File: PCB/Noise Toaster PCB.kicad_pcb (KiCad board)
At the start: 2 copper layers, 132.1 x 68.6 mm, 138 parts, among them Q1 2N5457, Q10 2N3906, Q2 2N3904, Q3 2N3904, Q4 2N3904, Q5 2N3904, Q6 2N3904, Q7 2N5457, Q8 2N5457, Q9 2N5457, U1 LM324, U2 LM324, U3 LM386, X4 WNS

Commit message: Shuffle things around
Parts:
- moved R6 0.76 mm to (182.3, 134.1)
- moved R41 0.63 mm to (113.7, 112.4)
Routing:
- net Net-(D1-A): track 37.5 -> 33.2 mm
- net /Attack Release Envelope Generator/X19: track 46.3 -> 42.2 mm
- net Net-(Q1-G): track 37.9 -> 38.7 mm
- net Net-(Q7-G): track 18.8 -> 19.4 mm
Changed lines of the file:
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@@
 	(footprint "Resistor_THT:R_Axial_DIN0207_L6.3mm_D2.5mm_P10.16mm_Horizontal"
 		(layer "F.Cu")
-		(at 182.276 133.377 180)
+		(at 182.276 134.139 180)
 		(descr "Resistor, Axial_DIN0207 series, Axial, Horizontal, pin pitch=10.16mm, 0.25W = 1/4W, length*diameter=6.3*2.5mm^2, http://cdn-reichelt.de/documents/datenblatt/B400/1_4W%23YAG.pdf")
 		(tags "Resistor Axial_DIN0207 series Axial Horizontal pin pitch 10.16mm 0.25W = 1/4W length 6.3mm diameter 2.5mm")
@@
 	(footprint "Resistor_THT:R_Axial_DIN0207_L6.3mm_D2.5mm_P10.16mm_Horizontal"
 		(layer "F.Cu")
-		(at 113.061 112.422 180)
+		(at 113.696 112.422 180)
 		(descr "Resistor, Axial_DIN0207 series, Axial, Horizontal, pin pitch=10.16mm, 0.25W = 1/4W, length*diameter=6.3*2.5mm^2, http://cdn-reichelt.de/documents/datenblatt/B400/1_4W%23YAG.pdf")
 		(tags "Resistor Axial_DIN0207 series Axial Horizontal pin pitch 10.16mm 0.25W = 1/4W length 6.3mm diameter 2.5mm")
@@
 	)
 	(segment
-		(start 94.011 104.167)
-		(end 98.456 108.612)
+		(start 81.057 103.405)
+		(end 84.201 103.405)
 		(width 0.5)
 		(layer "F.Cu")
@@
 	)
 	(segment
-		(start 94.011 102.897)
-		(end 94.011 104.167)
+		(start 100.107 108.612)
+		(end 102.647 111.152)
 		(width 0.5)
 		(layer "F.Cu")
@@
 	)
 	(segment
-		(start 91.598 100.484)
-		(end 94.011 102.897)
+		(start 98.456 108.612)
+		(end 100.107 108.612)
 		(width 0.5)
 		(layer "F.Cu")
@@
 	)
 	(segment
-		(start 111.791 111.152)
-		(end 113.061 112.422)
+		(start 94.011 104.167)
+		(end 98.456 108.612)
 		(width 0.5)
 		(layer "F.Cu")
@@
 	)
 	(segment
-		(start 81.057 103.405)
-		(end 84.201 103.405)
+		(start 102.647 111.152)
+		(end 112.426 111.152)
 		(width 0.5)
 		(layer "F.Cu")
@@
 	)
 	(segment
-		(start 98.456 108.612)
-		(end 100.361 108.612)
+		(start 91.598 102.262)
+		(end 91.598 100.484)
 		(width 0.5)
 		(layer "F.Cu")
@@
 	)
 	(segment
-		(start 91.598 102.262)
-		(end 91.598 100.484)
+		(start 89.693 104.167)
+		(end 91.598 102.262)
 		(width 0.5)
 		(layer "F.Cu")
@@
 	)
 	(segment
-		(start 89.693 104.167)
-		(end 91.598 102.262)
+		(start 112.426 111.152)
+		(end 113.696 112.422)
 		(width 0.5)
 		(layer "F.Cu")
@@
 	)
 	(segment
-		(start 84.963 104.167)
-		(end 89.693 104.167)
+		(start 94.011 102.897)
+		(end 94.011 104.167)
 		(width 0.5)
 		(layer "F.Cu")
@@
 	)
 	(segment
-		(start 100.361 108.612)
-		(end 102.901 111.152)
+		(start 84.963 104.167)
+		(end 89.693 104.167)
 		(width 0.5)
 		(layer "F.Cu")
@@
 	)
 	(segment
-		(start 102.901 111.152)
-		(end 111.791 111.152)
+		(start 91.598 100.484)
+		(end 94.011 102.897)
 		(width 0.5)
 		(layer "F.Cu")
@@
 	(segment
 		(start 114.331 112.422)
-		(end 113.061 112.422)
+		(end 113.696 112.422)
 		(width 0.5)
 		(layer "B.Cu")
@@
 	)
 	(segment
-		(start 113.061 112.422)
-		(end 113.676 113.037)
+		(start 121.316 105.437)
+		(end 114.331 112.422)
 		(width 0.5)
 		(layer "B.Cu")
@@
 	)
 	(segment
-		(start 113.676 124.507)
-		(end 112.426 125.757)
+		(start 113.676 112.442)
+		(end 113.676 124.507)
 		(width 0.5)
 		(layer "B.Cu")
@@
 	)
 	(segment
-		(start 113.676 113.037)
-		(end 113.676 124.507)
+		(start 113.696 112.422)
+		(end 113.676 112.442)
 		(width 0.5)
 		(layer "B.Cu")
@@
 	)
 	(segment
-		(start 121.316 105.437)
-		(end 114.331 112.422)
+		(start 113.676 124.507)
+		(end 112.426 125.757)
 		(width 0.5)
 		(layer "B.Cu")
@@
 	)
 	(segment
-		(start 184.8922 119.915)
-		(end 181.2346 119.915)
-		(width 0.5)
-		(layer "F.Cu")
-		(net "/G2")
-	)
-	(segment
 		(start 160.686 105.564)
 		(end 156.027 105.564)
@@
 	)
 	(segment
+		(start 181.2346 119.915)
+		(end 184.8922 119.915)
+		(width 0.5)
+		(layer "B.Cu")
+		(net "/G2")
+	)
+	(segment
 		(start 175.291 104.167)
 		(end 175.291 111.787)
@@
 	)
 	(segment
-		(start 187.229 113.565)
+		(start 183.038 114.2)
 		(end 185.451 111.787)
 		(width 0.5)
@@
 	)
 	(segment
-		(start 187.229 120.677)
-		(end 187.229 113.565)
-		(width 0.5)
-		(layer "F.Cu")
-		(net "Net-(D1-A)")
-	)
-	(segment
-		(start 186.213 121.693)
-		(end 187.229 120.677)
+		(start 179.9846 123.175627)
+		(end 181.467227 121.693)
 		(width 0.5)
 		(layer "F.Cu")
@@
 	)
 	(segment
-		(start 179.9846 123.175627)
-		(end 181.467227 121.693)
+		(start 181.467227 121.693)
+		(end 183.038 120.122227)
 		(width 0.5)
 		(layer "F.Cu")
@@
 	)
 	(segment
-		(start 181.467227 121.693)
-		(end 186.213 121.693)
+		(start 183.038 120.122227)
+		(end 183.038 114.2)
 		(width 0.5)
 		(layer "F.Cu")
@@
 	)
 	(segment
-		(start 83.405 98.517)
-		(end 96.997 98.517)
-		(width 0.5)
-		(layer "F.Cu")
-		(net "/Attack Release Envelope Generator/X19")
-	)
-	(segment
-		(start 96.997 98.517)
-		(end 102.647 104.167)
-		(width 0.5)
-		(layer "F.Cu")
-		(net "/Attack Release Envelope Generator/X19")
-	)
-	(segment
-		(start 103.536 105.056)
+		(start 106.711 105.437)
 		(end 103.536 108.612)
 		(width 0.5)
@@
 	)
 	(segment
-		(start 81.057 100.865)
-		(end 83.405 98.517)
+		(start 118.776 105.437)
+		(end 106.711 105.437)
 		(width 0.5)
 		(layer "F.Cu")
@@
 	)
 	(segment
-		(start 106.711 105.437)
+		(start 88.804 108.612)
 		(end 103.536 108.612)
 		(width 0.5)
-		(layer "F.Cu")
-		(net "/Attack Release Envelope Generator/X19")
-	)
-	(segment
-		(start 118.776 105.437)
-		(end 106.711 105.437)
-		(width 0.5)
-		(layer "F.Cu")
+		(layer "B.Cu")
 		(net "/Attack Release Envelope Generator/X19")
 	)
 	(segment
-		(start 102.647 104.167)
-		(end 103.536 105.056)
+		(start 81.057 100.865)
+		(end 88.804 108.612)
 		(width 0.5)
-		(layer "F.Cu")
+		(layer "B.Cu")
 		(net "/Attack Release Envelope Generator/X19")
 	)
@@
 	)
 	(segment
-		(start 167.036 134.012)
-		(end 168.306 135.282)
+		(start 167.798 123.392483)
+		(end 167.036 124.154483)
 		(width 0.5)
 		(layer "F.Cu")
@@
 	)
 	(segment
-		(start 168.306 135.282)
-		(end 180.371 135.282)
+		(start 182.276 135.028)
+		(end 182.276 134.139)
 		(width 0.5)
 		(layer "F.Cu")
@@
 	)
 	(segment
-		(start 167.798 123.392483)
-		(end 167.036 124.154483)
+		(start 169.068 136.044)
+		(end 181.26 136.044)
 		(width 0.5)
 		(layer "F.Cu")
@@
 	)
 	(segment
-		(start 180.371 135.282)
-		(end 182.276 133.377)
+		(start 167.036 134.012)
+		(end 169.068 136.044)
+		(width 0.5)
+		(layer "F.Cu")
+		(net "Net-(Q1-G)")
+	)
+	(segment
+		(start 181.26 136.044)
+		(end 182.276 135.028)
 		(width 0.5)
 		(layer "F.Cu")
@@
 	)
 	(segment
-		(start 172.116 133.377)
-		(end 170.846 133.377)
+		(start 170.084 134.139)
+		(end 167.671 136.552)
 		(width 0.5)
 		(layer "B.Cu")
@@
 	)
 	(segment
-		(start 167.671 136.552)
-		(end 167.671 137.822)
+		(start 172.116 134.139)
+		(end 170.084 134.139)
 		(width 0.5)
 		(layer "B.Cu")
@@
 	)
 	(segment
-		(start 170.846 133.377)
-		(end 167.671 136.552)
+		(start 167.671 136.552)
+		(end 167.671 137.822)
 		(width 0.5)
 		(layer "B.Cu")
@@
 	)
 	(segment
-		(start 101.631 113.692)
-		(end 102.901 112.422)
+		(start 97.186 114.962)
+		(end 98.456 113.692)
 		(width 0.5)
 		(layer "F.Cu")
@@
 	)
 	(segment
-		(start 98.456 113.692)
-		(end 101.631 113.692)
+		(start 102.266 113.692)
+		(end 103.536 112.422)
 		(width 0.5)
 		(layer "F.Cu")
@@
 	)
 	(segment
-		(start 97.186 114.962)
-		(end 98.456 113.692)
+		(start 98.456 113.692)
+		(end 102.266 113.692)
 		(width 0.5)
 		(layer "F.Cu")

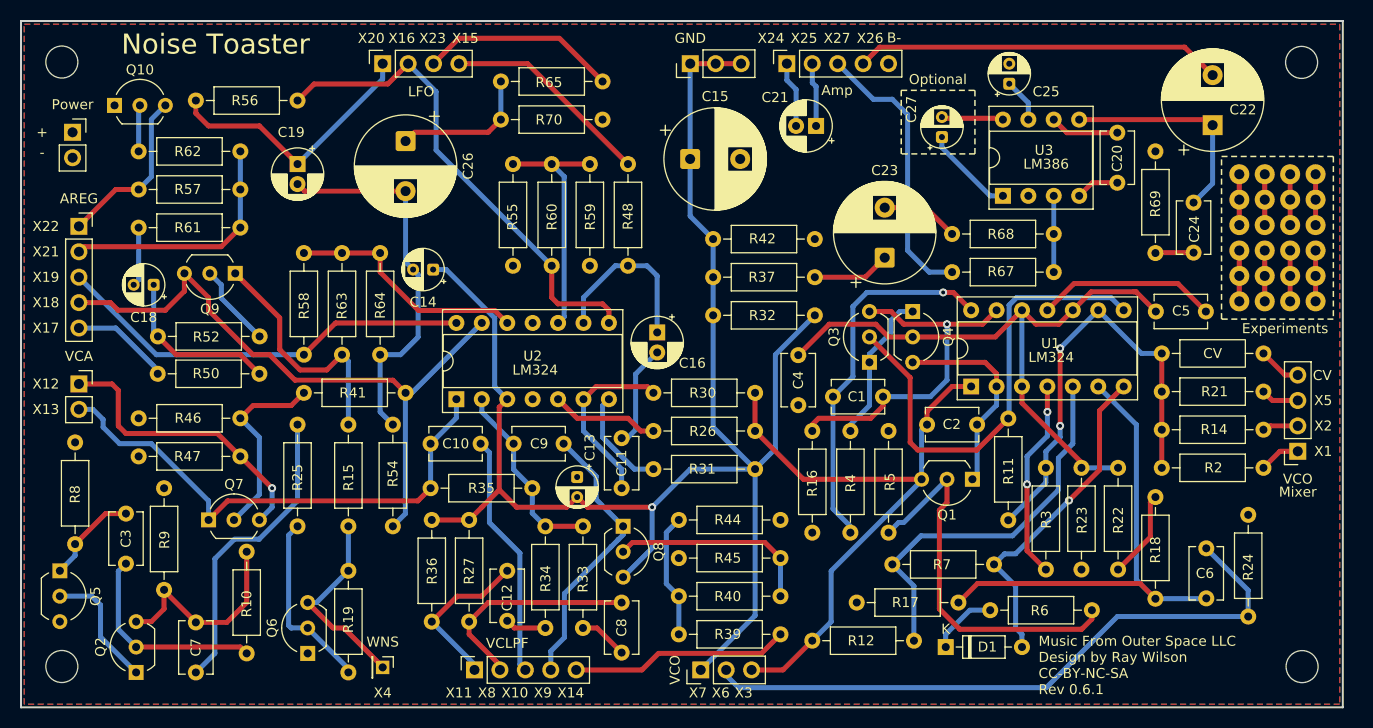
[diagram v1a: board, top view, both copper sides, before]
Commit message: Added VCF mod back
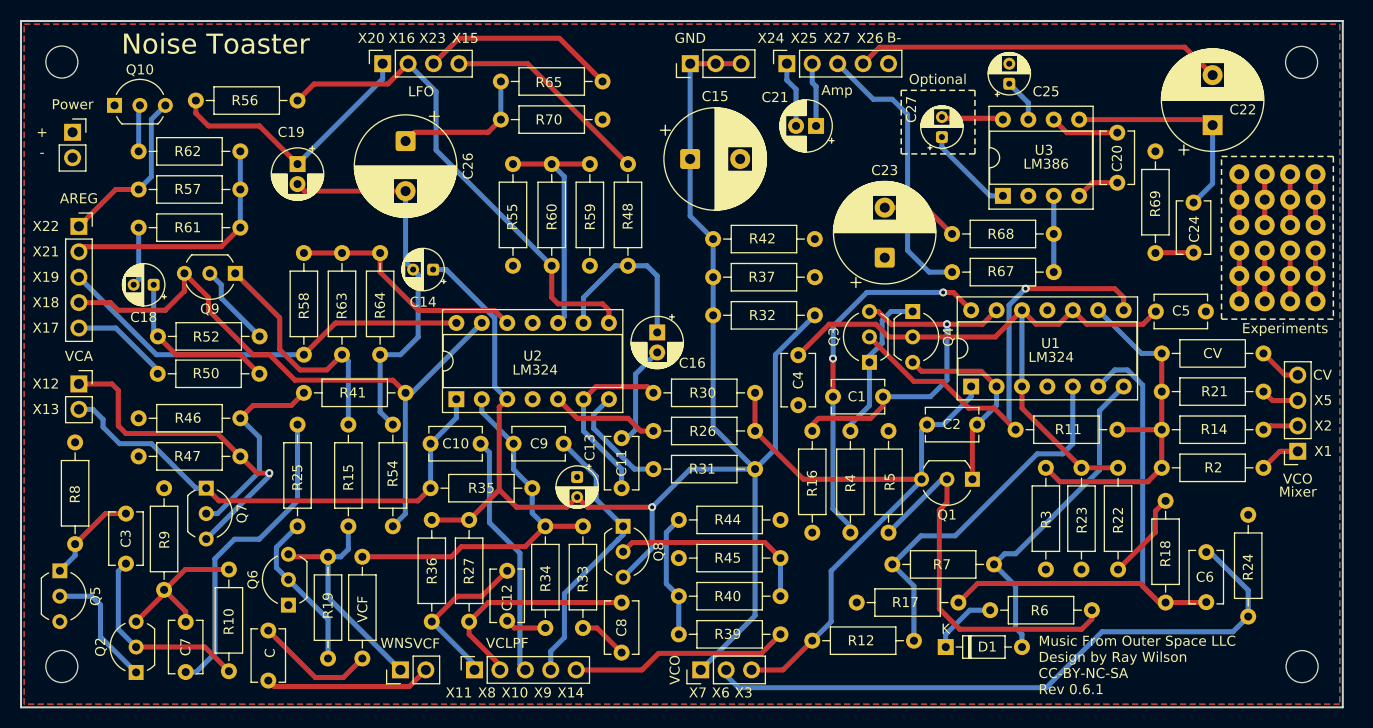
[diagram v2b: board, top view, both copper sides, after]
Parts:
- added C: 0.1 uF, Capacitor_THT:C_Disc_D5.1mm_W3.2mm_P5.00mm, F.Cu at (100.0, 136.2)
- added VCF: 3 M, Resistor_THT:R_Axial_DIN0207_L6.3mm_D2.5mm_P10.16mm_Horizontal, F.Cu at (109.4, 139.0)
- WNS: renamed from X4; footprint Connector_PinHeader_2.00mm:PinHeader_1x01_P2.00mm_Vertical -> Connector_PinHeader_2.54mm:PinHeader_1x02_P2.54mm_Vertical
- moved R11 14.2 mm to (184.8, 116.1), turned to 180 degrees
- moved Q6 5.20 mm to (102.0, 133.6)
- moved Q7 3.18 mm to (93.8, 121.9), turned to -90 degrees
- moved R10 2.51 mm to (96.0, 130.1)
- moved R19 2.47 mm to (105.9, 128.8)
- moved WNS 1.79 mm to (113.2, 140.1), turned to 90 degrees
- moved R18 1.09 mm to (189.6, 133.4)
- moved C7 1.02 mm to (91.7, 135.3)
- moved C6 0.38 mm to (193.7, 128.3)
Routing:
- net (no net): track 45.0 -> 73.8 mm
- net B+: track 59.0 -> 31.3 mm, vias 2 -> 0
- net Net-(U2A--): track 19.1 -> 38.6 mm
- net B-: track 106.2 -> 88.1 mm
- net Net-(U1C--): track 44.3 -> 36.8 mm, vias 2 -> 0
- net Net-(U1B--): track 49.8 -> 55.1 mm
- net Net-(Q2-C): track 20.7 -> 15.8 mm
- net /Front Panel/X12: track 29.4 -> 34.0 mm
- net /WNS: track 19.9 -> 23.0 mm
- net /FO: track 52.6 -> 49.9 mm
- net Net-(Q3-B): track 47.2 -> 44.9 mm, vias 0 -> 1
- net Net-(Q6-B): track 18.4 -> 16.2 mm
- net Net-(U1B-+): track 39.1 -> 37.3 mm
- net Net-(Q7-G): track 19.4 -> 20.6 mm
- net Net-(Q2-B): track 20.7 -> 19.7 mm
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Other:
- board text added: "VCF"

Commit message: Moved filtering caps closer to OPamps
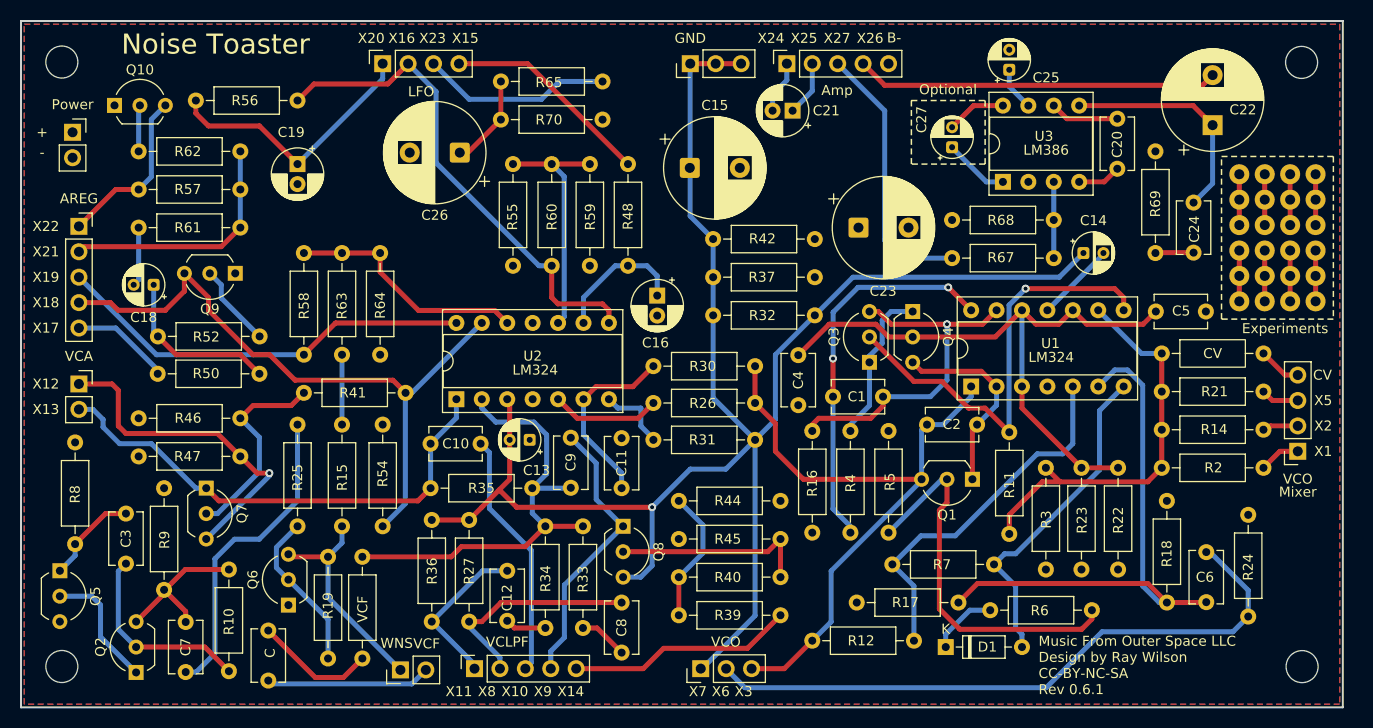
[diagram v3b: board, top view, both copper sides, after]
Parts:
- moved C14 65.0 mm to (181.4, 98.5), turned to 0 degrees
- moved R11 15.0 mm to (174.0, 126.5), turned to 90 degrees
- moved C13 6.02 mm to (126.1, 117.1), turned to 180 degrees
- moved C26 5.54 mm to (119.1, 88.4), turned to 180 degrees
- moved C23 3.99 mm to (159.0, 95.9), turned to 0 degrees
- moved C16 3.68 mm to (138.8, 102.7)
- moved R31 2.92 mm to (138.5, 117.1)
- moved C21 2.80 mm to (152.4, 84.2)
- moved R26 2.79 mm to (148.6, 113.4)
- moved R30 2.67 mm to (148.6, 109.8)
- moved R39 1.91 mm to (151.2, 134.6)
- moved R40 1.91 mm to (141.0, 130.8)
- moved R44 1.91 mm to (141.0, 123.2)
- moved R45 1.90 mm to (141.0, 127.0)
- moved C27 1.44 mm to (168.3, 87.9)
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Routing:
- net B-: track 88.1 -> 30.9 mm
- net B+: track 31.3 -> 13.9 mm
- net GND: track 159.5 -> 170.7 mm
- net Net-(U2A--): track 38.6 -> 45.9 mm
- net Net-(R31-Pad1): track 11.2 -> 7.26 mm
- net Net-(U1C--): track 36.8 -> 40.6 mm
- net Net-(C26-Pad1): track 13.0 -> 9.29 mm
- net Net-(U2C--): track 17.3 -> 13.6 mm
- net /RMP: track 62.6 -> 65.3 mm
- net Net-(C27-Pad1): track 9.14 -> 6.53 mm
- net /Audio Amplifier/X24: track 6.60 -> 5.29 mm
- net Net-(C1-Pad2): track 36.6 -> 37.9 mm
- net /WNS: track 23.0 -> 22.0 mm
- net Net-(R39-Pad2): track 12.5 -> 13.4 mm
- net /Audio Amplifier/X27: track 28.0 -> 27.1 mm
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
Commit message: Changed Q1 Q7 Q8 Q9 Drain Source Pads
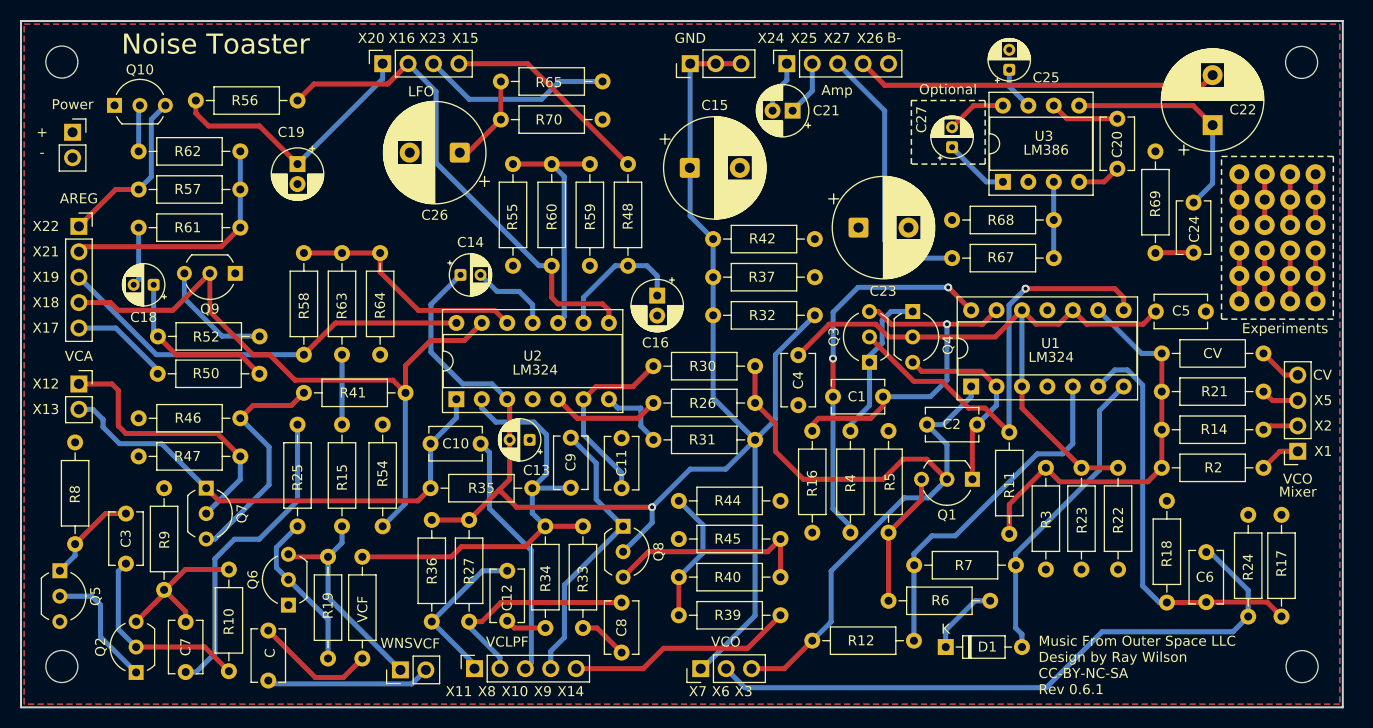
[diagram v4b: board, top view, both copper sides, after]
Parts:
- moved C14 62.3 mm to (119.2, 100.6)
- moved R17 32.3 mm to (201.2, 134.8), turned to 90 degrees
- moved R6 20.3 mm to (162.0, 133.2), turned to 0 degrees
- moved R7 2.19 mm to (164.5, 129.6)
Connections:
- Q1 pad 2: Net-(Q1-G) -> /RMP
- Q1 pad 3: /RMP -> Net-(Q1-G)
- Q7 pad 2: Net-(Q7-G) -> /Front Panel/X12
- Q7 pad 3: /Front Panel/X12 -> Net-(Q7-G)
- Q8 pad 2: Net-(Q8-G) -> GND
- Q8 pad 3: GND -> Net-(Q8-G)
- Q9 pad 2: Net-(Q9-G) -> /ARG
- Q9 pad 3: /ARG -> Net-(Q9-G)
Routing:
- net Net-(Q1-G): track 38.7 -> 13.5 mm
- net GND: track 170.7 -> 155.8 mm
- net Net-(U1B--): track 55.1 -> 40.8 mm
- net /RMP: track 65.3 -> 72.5 mm
- net /Front Panel/X12: track 34.0 -> 28.3 mm, vias 1 -> 0
- net Net-(Q9-G): track 8.36 -> 11.6 mm
- net Net-(Q7-G): track 20.6 -> 23.8 mm
- net Net-(D1-A): track 33.2 -> 30.8 mm
- net Net-(U1B-+): track 37.3 -> 34.8 mm
- net /ARG: track 66.0 -> 68.0 mm
- net Net-(Q8-G): track 20.1 -> 21.1 mm
- net Net-(D1-K): track 6.71 -> 7.34 mm
- net /Front Panel/X6: track 64.4 -> 63.9 mm
- net /Front Panel/X8: track 22.0 -> 21.5 mm
